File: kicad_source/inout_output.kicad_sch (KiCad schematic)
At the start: 9 parts, among them J13 Conn_01x02, J14 Conn_01x02, J18 Conn_01x02, U14 ITS4200S-ME-P, U15 ITS4200S-ME-P

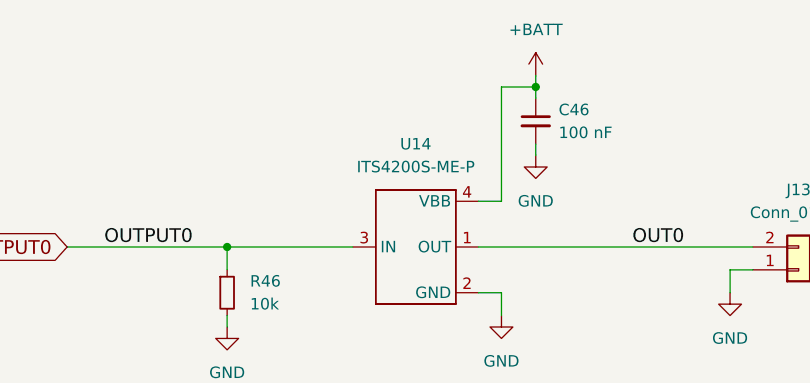
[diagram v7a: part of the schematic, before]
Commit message: checked supply voltage of parts
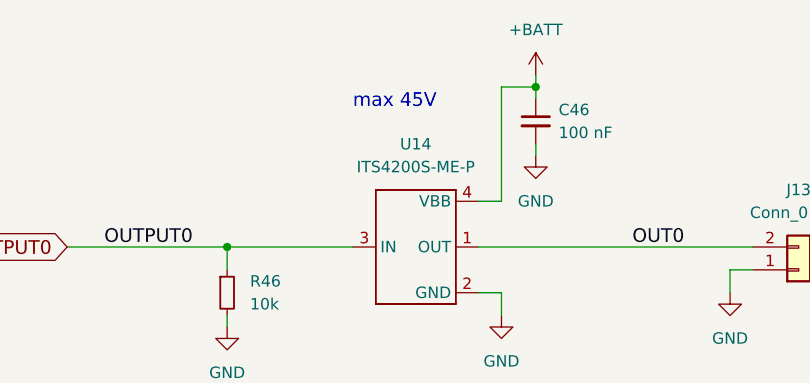
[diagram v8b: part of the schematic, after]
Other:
- note added: "max 45V"
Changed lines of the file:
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@@
+    (effects (font (size 1.524 1.524)) (justify left bottom))
+  )
+  (text "max 45V" (at 99.06 46.99 0)
     (effects (font (size 1.524 1.524)) (justify left bottom))
   )
